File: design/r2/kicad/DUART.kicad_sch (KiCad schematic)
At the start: 17 parts, among them IC4 XR68C681CJTR-F, J1 UART_A, J2 UART_B, J4 Conn_01x06, J7 Conn_01x01_Male, Q1 3.6864MHz

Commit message: Complete Kicad 7 migration
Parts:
- J1, J2: symbol Connector:Conn_01x06_Male -> Connector:Conn_01x06_Pin
- J7: symbol Connector:Conn_01x01_Male -> Connector:Conn_01x01_Pin
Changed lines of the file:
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@@
     )
   )
-  (symbol (lib_id "Connector:Conn_01x06_Male") (at 31.75 148.59 0) (unit 1)
+  (symbol (lib_id "Connector:Conn_01x06_Pin") (at 31.75 148.59 0) (unit 1)
     (in_bom yes) (on_board yes) (dnp no)
     (property "Reference" "J1" (at 34.4932 138.9126 0)
@@
     )
   )
-  (symbol (lib_id "Connector:Conn_01x06_Male") (at 31.75 170.18 0) (unit 1)
+  (symbol (lib_id "Connector:Conn_01x06_Pin") (at 31.75 170.18 0) (unit 1)
     (in_bom yes) (on_board yes) (dnp no)
     (property "Reference" "J2" (at 34.4932 160.5026 0)
@@
     )
   )
-  (symbol (lib_id "Connector:Conn_01x01_Male") (at 101.6 143.51 180) (unit 1)
+  (symbol (lib_id "Connector:Conn_01x01_Pin") (at 101.6 143.51 180) (unit 1)
     (in_bom yes) (on_board yes) (dnp no)
     (property "Reference" "J7" (at 99.06 139.7 0)

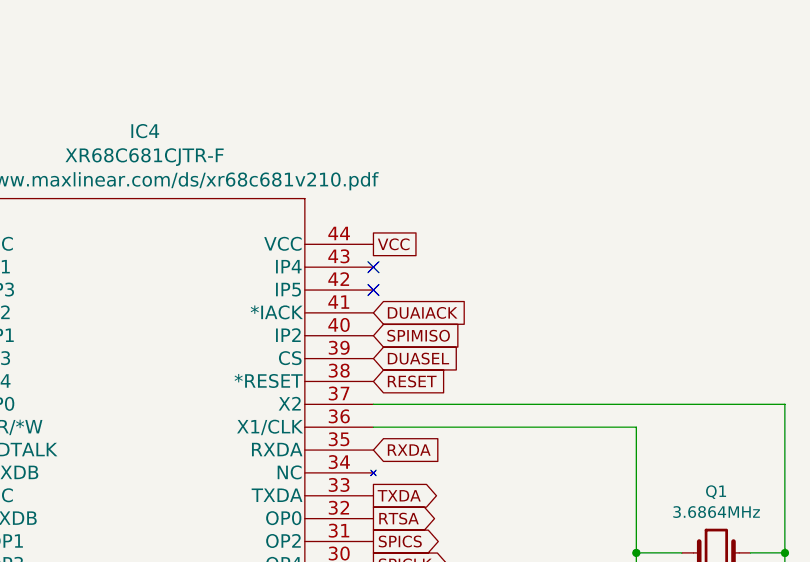
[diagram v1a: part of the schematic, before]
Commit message: Feature/swap tx rx again (#395)
* Swap TX/RX & CTS/RTS silkscreen r2

* Swap over labels
* Add arrows
* Some board tidy up

* Swap TX/RX & CTS/RTS silkscreen r2020

    * Swap over labels
    * Add arrows
    * Some board tidy up
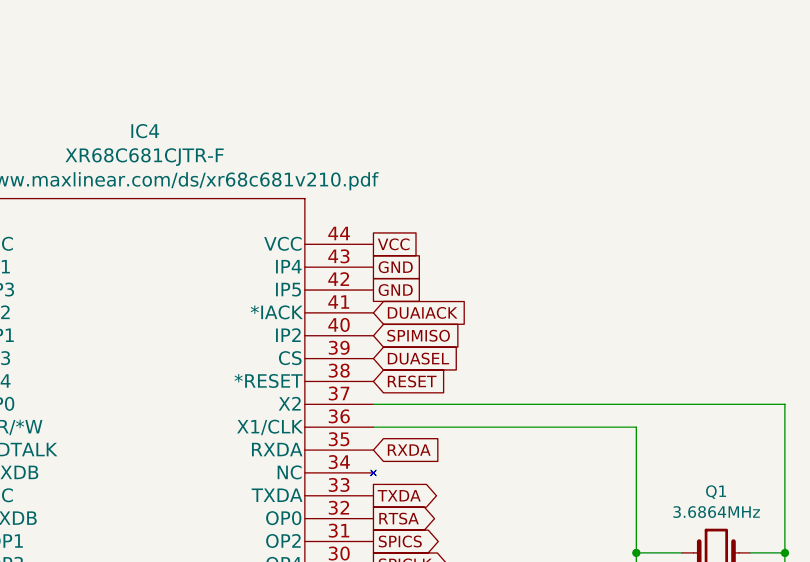
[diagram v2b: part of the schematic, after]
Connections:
- net GND: now also IC4.42 (IP5), IC4.43 (IP4)
- no-connect marks 2 -> 0
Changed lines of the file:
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@@
   (title_block
     (title "ROSCO_M68K GENERAL PURPOSE MC68010 COMPUTER")
-    (date "2023-08-17")
+    (date "2023-12-10")
     (rev "2.13-DEV")
     (company "The Really Old-School Company Limited")
@@
   (junction (at 191.77 80.01) (diameter 0) (color 0 0 0 0)
   )
-  (no_connect (at 162.56 50.8))
-  (no_connect (at 162.56 48.26))
   (wire (pts (xy 92.71 52.07) (xy 86.36 52.07))
     (stroke (width 0) (type default))
@@
     )
   )
+  (global_label "GND" (shape passive) (at 162.56 50.8 0) (fields_autoplaced)
+    (effects (font (size 1.27 1.27)) (justify left))
+    (property "Intersheetrefs" "${INTERSHEET_REFS}" (at 167.809 50.8 0)
+      (effects (font (size 1.27 1.27)) (justify left) hide)
+    )
+  )
   (global_label "VCCUB" (shape passive) (at 241.3 143.51 180) (fields_autoplaced)
     (effects (font (size 1.27 1.27)) (justify right))
@@
     )
   )
+  (global_label "GND" (shape passive) (at 162.56 48.26 0) (fields_autoplaced)
+    (effects (font (size 1.27 1.27)) (justify left))
+    (property "Intersheetrefs" "${INTERSHEET_REFS}" (at 167.809 48.26 0)
+      (effects (font (size 1.27 1.27)) (justify left) hide)
+    )
+  )

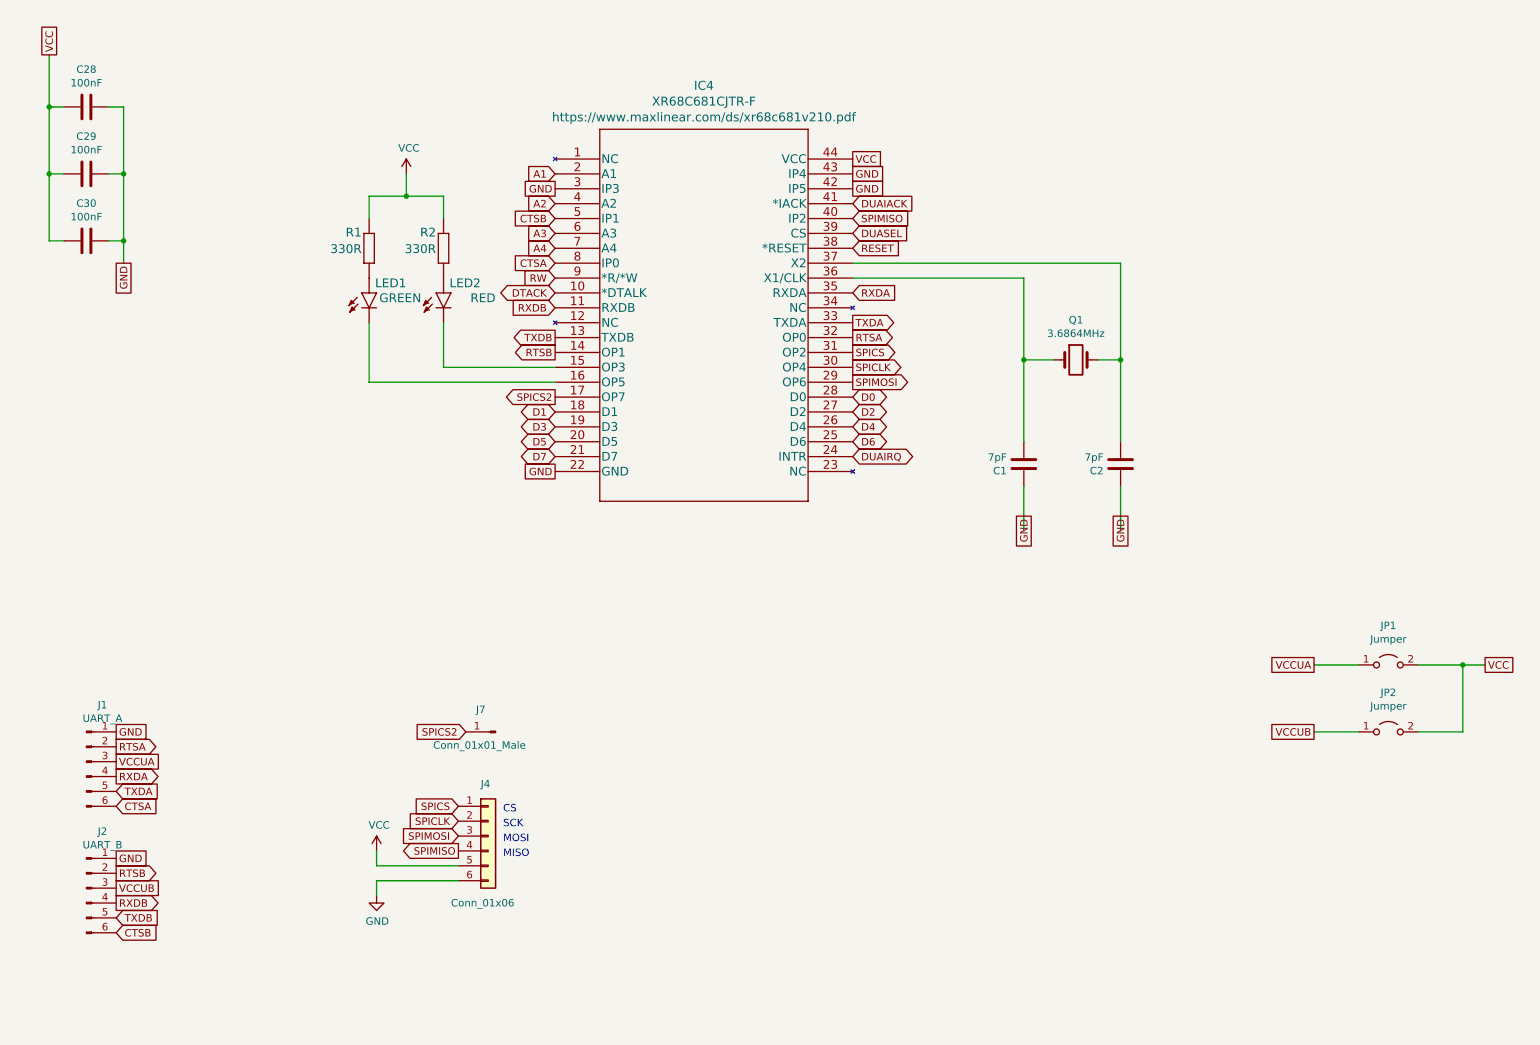
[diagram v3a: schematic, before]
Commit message: Feature/smd birdseed (#427)
* GAL changes to better support coprocessor

* Update designs for copro GAL change

* Revert accidental DUARTSEL changes

* Re-add mistakenly-removed polarity symbols

* Tentative r2 SMD design

* Resize tiny resistors

* More address lines into GALs

* Reroute for FTDI

* prod

* Correct FT2232HL part number

* Mask expansion and silk tidy after first spin
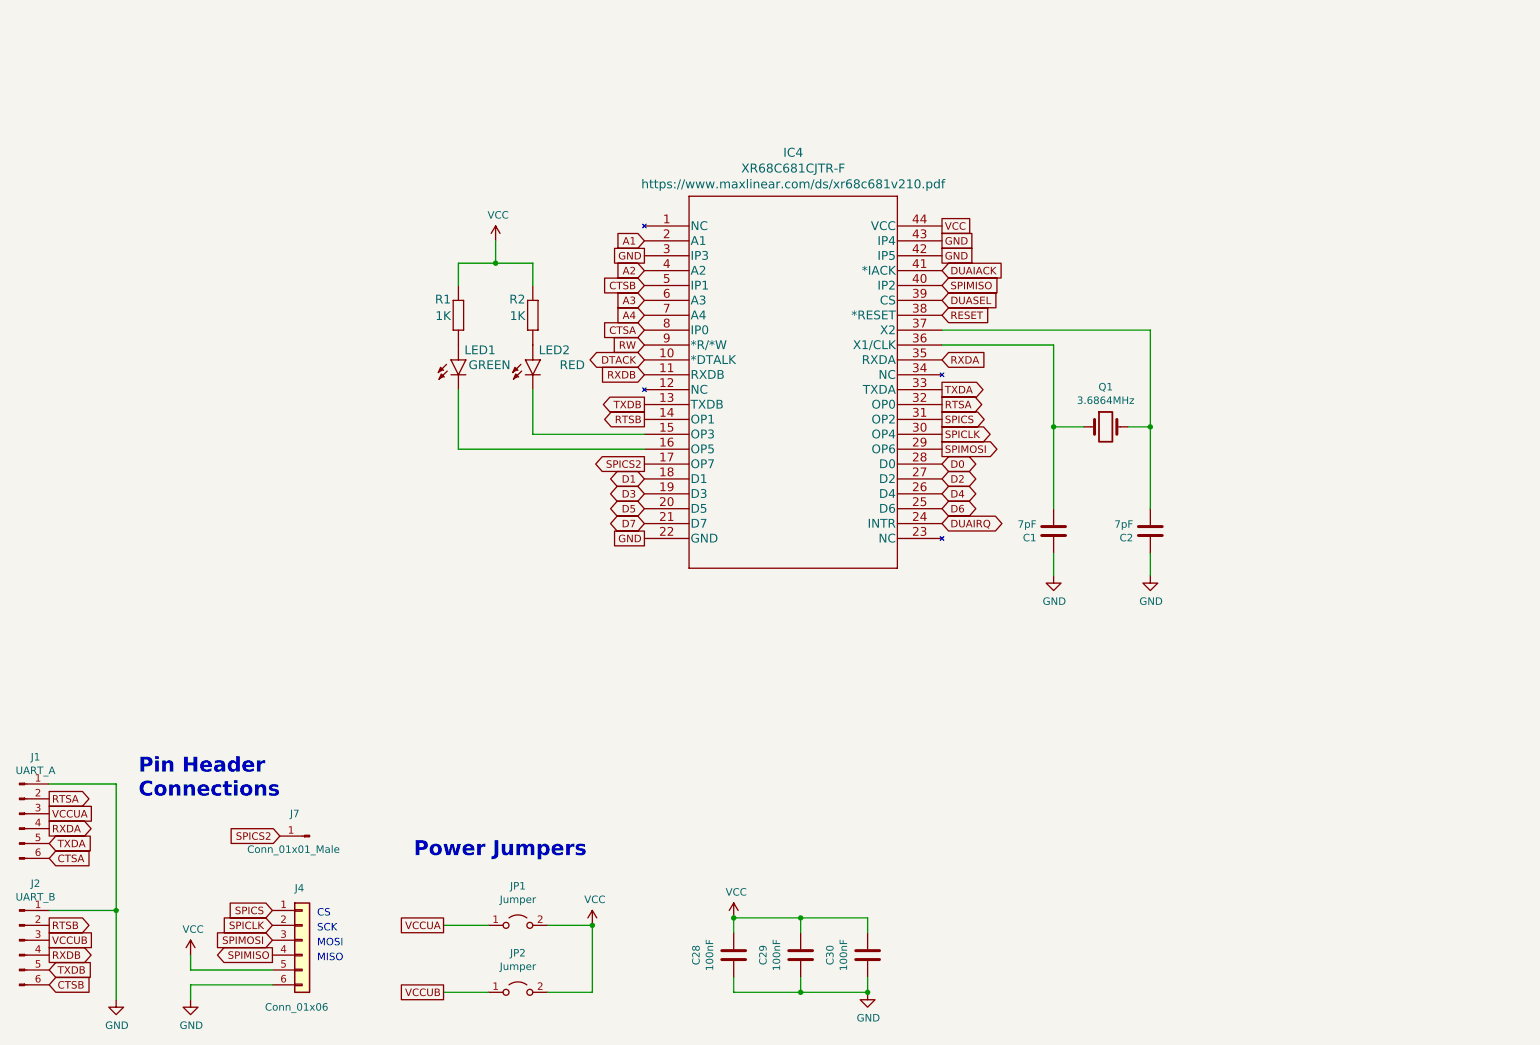
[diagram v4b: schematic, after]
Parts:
- C1, C2: footprint rosco_m68k:C2.5_or_3.5-3 -> Capacitor_SMD:C_0603_1608Metric
- C28, C29, C30: footprint rosco_m68k:C2.5-3 -> Capacitor_SMD:C_0603_1608Metric
- R1, R2: value 330R -> 1K; footprint rosco_m68k:0207_10 -> Resistor_SMD:R_0603_1608Metric
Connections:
- net GND: now also C28.2, C29.2, C30.2; no longer C28.1, C29.1, C30.1
- net VCC: now also C28.1, C29.1, C30.1; no longer C28.2, C29.2, C30.2
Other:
- note added: "Pin Header Connections"
- note added: "Power Jumpers"
- moved on the sheet: C1, C2, C28, C29, C30, IC4, J1, J2, J4, J7, JP1, JP2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
